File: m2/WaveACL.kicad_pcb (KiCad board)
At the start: 4 copper layers, 48 x 21 mm, 20 parts, among them J1 Conn_01x05, J2 Conn_01x02, J3 Conn_01x02, J4 Conn_01x02, J5 Conn_01x02, U1 LED2000, U2 LPC812M001JDH16

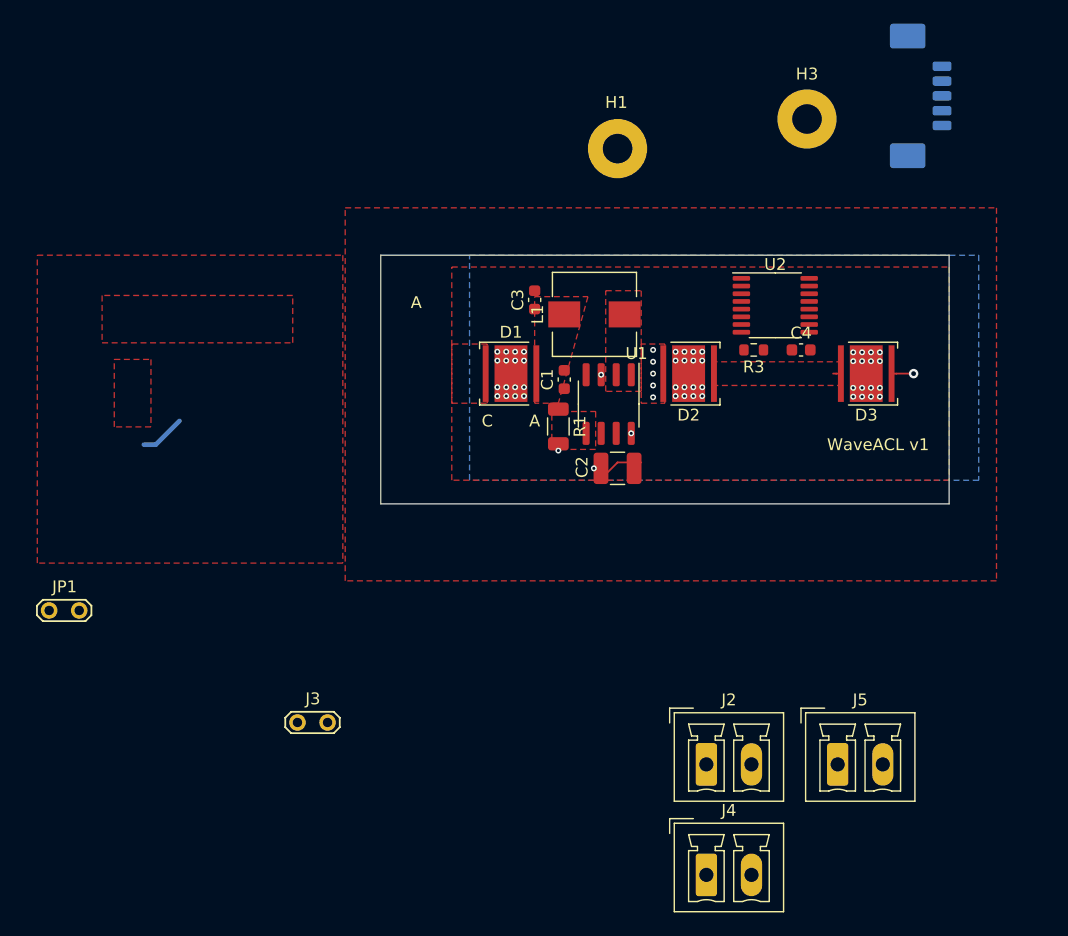
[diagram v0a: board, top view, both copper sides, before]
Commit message: Mark2 updates
- add I2C temp. sensor
- add voltage regulator for uC
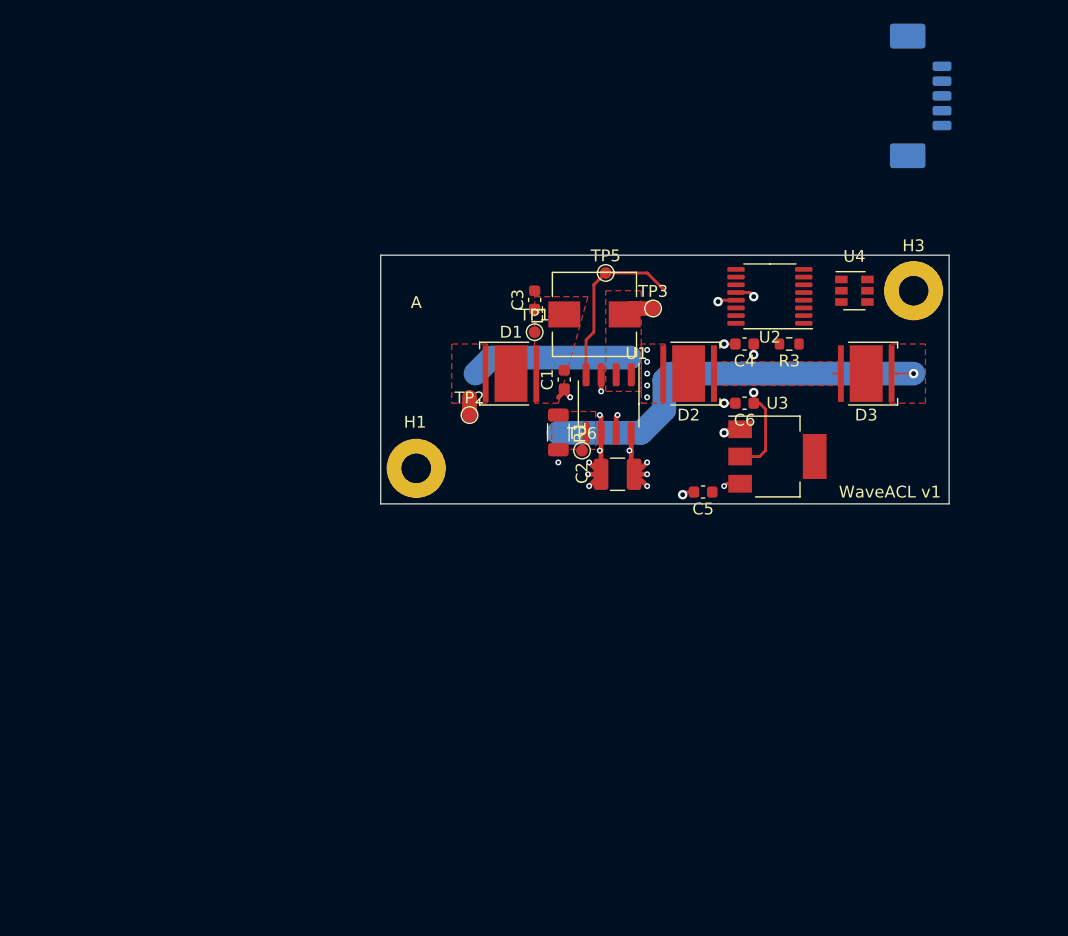
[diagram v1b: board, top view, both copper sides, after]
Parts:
- removed J2, J4, J5: Conn_01x02, Connector_Phoenix_MC:PhoenixContact_MCV_1,5_2-G-3.81_1x02_P3.81mm_Vertical
- removed J3: Conn_01x02, TestPoint:TestPoint_2Pads_Pitch2.54mm_Drill0.8mm
- removed JP1: Jumper_NO_Small, TestPoint:TestPoint_2Pads_Pitch2.54mm_Drill0.8mm
- added C5: 100n, Capacitor_SMD:C_0603_1608Metric, F.Cu at (165.2, 49.0)
- added C6: 100n, Capacitor_SMD:C_0603_1608Metric, F.Cu at (168.7, 41.5)
- added TP1: TestPoint, TestPoint:TestPoint_Pad_D1.0mm, F.Cu at (151.0, 35.5)
- added TP2: TestPoint, TestPoint:TestPoint_Pad_D1.0mm, F.Cu at (145.5, 42.5)
- added TP3: TestPoint, TestPoint:TestPoint_Pad_D1.0mm, F.Cu at (161.0, 33.5)
- added TP5: TestPoint, TestPoint:TestPoint_Pad_D1.0mm, F.Cu at (157.0, 30.5)
- added TP6: TestPoint, TestPoint:TestPoint_Pad_D1.0mm, F.Cu at (155.0, 45.5)
- added U3: LD1117S33TR_SOT223, Package_TO_SOT_SMD:SOT-223-3_TabPin2, F.Cu at (171.5, 46.0)
- added U4: TMP100, Package_TO_SOT_SMD:SOT-23-6, F.Cu at (178.0, 32.0)
- D1, D2, D3: footprint LED_SMD:LED_Cree-XHP50_6V -> fkl-footprints:LED_Cree-XHP50_6V
- moved H1 31.9 mm to (141.0, 47.0)
- moved H3 17.1 mm to (183.0, 32.0)
- moved C4 4.80 mm to (168.7, 36.5), turned to 180 degrees
- moved R3 3.04 mm to (172.5, 36.5)
- moved U2 0.88 mm to (170.9, 32.5), turned to 180 degrees
- moved C2 0.50 mm to (158.0, 47.5)
- moved R1 0.50 mm to (153.0, 44.0)
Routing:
- net /LED-: track 1.86 -> 35.4 mm
- net +3V3: track 0.00 -> 19.0 mm, vias 0 -> 3
- net VCC: track 4.60 -> 19.5 mm, vias 2 -> 7
- net PWM: track 0.00 -> 14.9 mm
- net (no net): track 0.00 -> 13.6 mm
- net GND: track 7.50 -> 16.2 mm, vias 50 -> 12
- net Net-(J3-Pad1): track 3.41 -> 0.00 mm
- net Net-(L1-Pad1): track 0.00 -> 2.61 mm
- net Net-(D1-Pad1): track 0.00 -> 1.50 mm
- added copper zone on F.Cu, net (none)
- added copper zone on In2.Cu, net VCC
- removed copper zone on B.Cu, net /HS1
- removed copper zone on F.Cu, net /HS1
- removed copper zone on F.Cu, net GND
- removed copper zone on In1.Cu, net GND
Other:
- board text removed: "C"

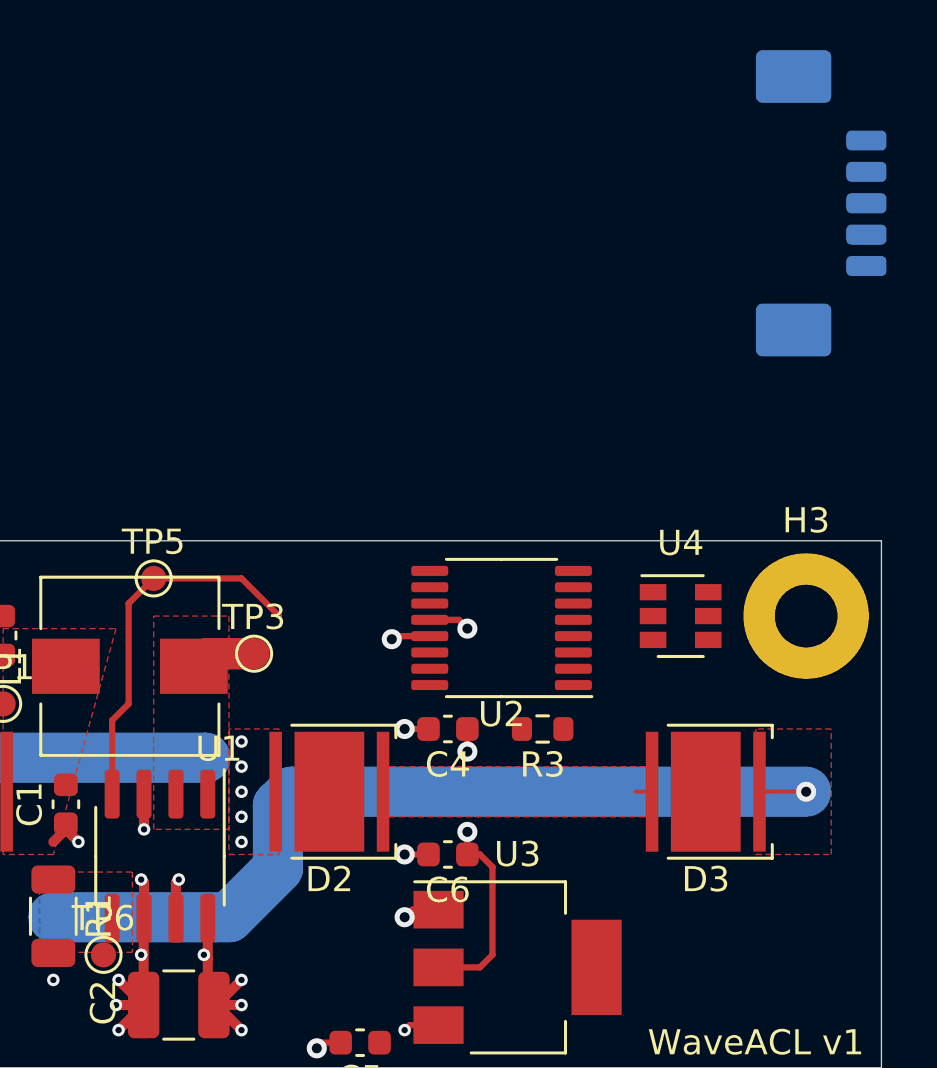
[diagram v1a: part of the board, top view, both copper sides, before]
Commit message: add SOICByte Footprint
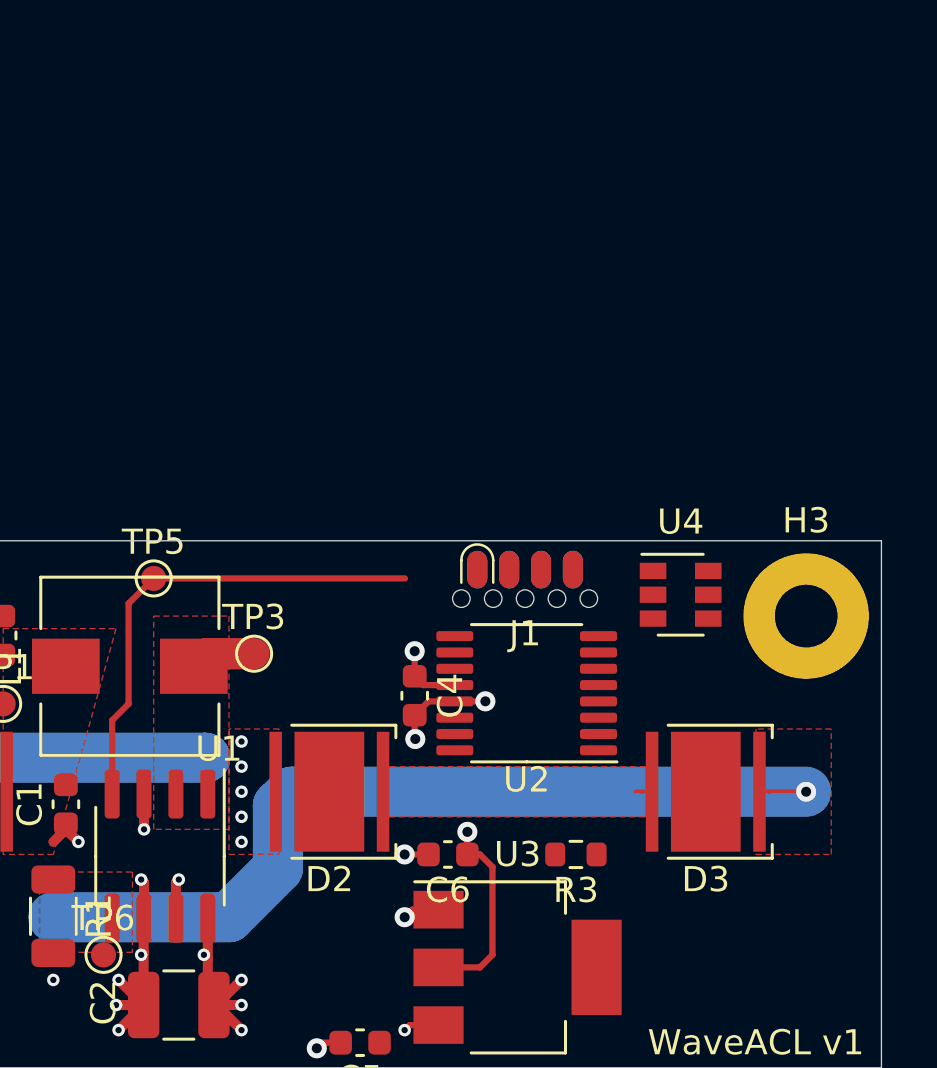
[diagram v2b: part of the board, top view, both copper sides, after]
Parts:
- J1: value Conn_01x05 -> Conn_01x08; footprint Connector_Molex:Molex_PicoBlade_53261-0571_1x05-1MP_P1.25mm_Horizontal -> fkl-footprints:Connector_SOICbite; moved to F.Cu
- moved J1 17.8 mm to (171.8, 29.4), turned to 180 degrees
- moved R3 5.17 mm to (173.8, 41.5)
- moved U2 2.79 mm to (171.9, 35.1)
- moved C4 1.87 mm to (167.4, 35.2), turned to 270 degrees
- moved U4 0.85 mm to (178.0, 31.1)
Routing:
- net PWM: track 14.9 -> 19.3 mm
- net GND: track 16.2 -> 17.7 mm
- net +3V3: vias 3 -> 2

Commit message: update m2
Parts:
- added C7: 100n, Capacitor_SMD:C_0603_1608Metric, F.Cu at (178.0, 34.0)
- C1: value 100n -> 1u
- D1, D2, D3: footprint fkl-footprints:LED_Cree-XHP50_6V -> fkl-footprints:LED_Cree-XLAMP-XM-L
- J1: value Conn_01x08 -> SOICBite
- moved TP1 4.92 mm to (146.5, 33.5)
- moved C3 1.95 mm to (151.0, 34.7)
- moved C1 0.27 mm to (153.5, 39.2)
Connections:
- J1 pad 1: /VTREF -> +3V3
- J1 pad 2: /SWDIO -> /RXD
- J1 pad 3: /SWCLK -> /TXD
- J1 pad 4: /~RESET -> GND
- J1 pad 5: GND -> /SWDIO
- J1 pad 7: Net-(J1-Pad7) -> /SWCLK
- J1 pad 8: Net-(J1-Pad8) -> /~RESET
- U4 pad 1: Net-(U4-Pad1) -> /SCK
- U4 pad 2: Net-(U4-Pad2) -> GND
- U4 pad 4: Net-(U4-Pad4) -> +3V3
- U4 pad 6: Net-(U4-Pad6) -> /SDA
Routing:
- net /~RESET: track 0.00 -> 9.41 mm, vias 0 -> 1
- net /SWCLK: track 0.00 -> 7.72 mm, vias 0 -> 1
- net GND: track 17.7 -> 23.7 mm, vias 12 -> 13
- net /SWDIO: track 0.00 -> 4.89 mm, vias 0 -> 1
- net PWM: track 19.3 -> 22.2 mm
- net +3V3: track 19.0 -> 20.7 mm
- net (no net): track 13.6 -> 14.1 mm
- net Net-(D1-Pad1): vias 5 -> 0
- added copper zone on F.Cu, net GND
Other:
- board text added: "WaveACL m2r0"
- board text removed: "WaveACL v1"

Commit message: updates
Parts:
- moved TP3 55.9 mm to (111.5, 59.5), turned to 180 degrees
- moved TP5 51.3 mm to (109.5, 50.0), turned to 180 degrees
- moved H1 30.3 mm to (171.0, 43.0)
- moved H3 29.2 mm to (156.0, 43.0)
- moved C2 25.2 mm to (139.0, 31.0), turned to 0 degrees
- moved C4 18.8 mm to (185.8, 38.9), turned to 180 degrees
- moved U1 18.1 mm to (139.8, 36.9), turned to 90 degrees
- moved TP6 18.0 mm to (142.0, 33.0), turned to 180 degrees
- moved L1 17.9 mm to (141.6, 44.5), turned to 0 degrees
- moved U4 16.0 mm to (179.8, 47.0), turned to 270 degrees
- moved C6 15.5 mm to (184.2, 41.0)
- moved R3 15.5 mm to (189.3, 41.0)
- moved U3 15.5 mm to (187.0, 45.5)
- moved J1 15.5 mm to (187.3, 29.4)
- moved U2 15.3 mm to (187.2, 35.1)
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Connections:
- H1 pad 1: /HS1 -> GND
- H3 pad 1: /HS1 -> GND
- U4 pad 3: Net-(U4-Pad3) -> GND
- U4 pad 5: Net-(U4-Pad5) -> GND
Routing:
- net /LED-: track 35.4 -> 13.1 mm, vias 1 -> 0
- net PWM: track 22.2 -> 8.74 mm
- net Net-(D2-Pad1): track 0.66 -> 11.4 mm
- net Net-(D1-Pad1): track 1.50 -> 10.7 mm
- net +3V3: track 20.7 -> 11.6 mm, vias 2 -> 1
- net GND: track 23.7 -> 18.2 mm, vias 13 -> 291
- net Net-(L1-Pad1): track 2.61 -> 0.71 mm
- net (no net): track 14.1 -> 12.9 mm
- removed copper zone on F.Cu, net (none)
- removed copper zone on F.Cu, net Net-(D1-Pad1)
- removed copper zone on F.Cu, net Net-(D2-Pad1)
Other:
- board size 48 x 21 mm -> 55 x 20 mm
- net class Default: clearance 0.2 -> 0.15
- net class current: clearance 0.2 -> 0.15; trace_width 1.25 -> 0.5
- rule trace_clearance: 0.2 -> 0.15
- rule via_min_size: 0.5 -> 0.6
- board text added: "WaveACL m2r1"
- board text removed: "WaveACL m2r0"

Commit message: update
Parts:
- added R2: R, Resistor_SMD:R_0603_1608Metric, F.Cu at (187.0, 41.8)
- added R4: R, Resistor_SMD:R_0603_1608Metric, F.Cu at (188.5, 41.8)
- added R5: R, Resistor_SMD:R_0603_1608Metric, F.Cu at (155.6, 54.9)
- added R6: R, Resistor_SMD:R_0603_1608Metric, F.Cu at (159.6, 54.9)
- added TP4: TestPoint, TestPoint:TestPoint_Pad_D1.0mm, F.Cu at (171.0, 39.0)
- added TP7: TestPoint, TestPoint:TestPoint_Pad_D1.0mm, F.Cu at (184.2, 41.5)
- U3: value LD1117S33TR_SOT223 -> TPS7A0533PDBV; footprint Package_TO_SOT_SMD:SOT-223-3_TabPin2 -> Package_TO_SOT_SMD:SOT-23-5
- U4: value TMP100 -> LM75B; footprint Package_TO_SOT_SMD:SOT-23-6 -> Package_DFN_QFN:DFN-8-1EP_3x2mm_P0.5mm_EP1.3x1.5mm
- moved TP5 37.6 mm to (147.0, 48.0)
- moved TP3 31.3 mm to (137.5, 42.0)
- moved C5 19.4 mm to (184.0, 46.5), turned to 270 degrees
- moved C6 7.98 mm to (190.0, 46.5), turned to 270 degrees
- moved C7 1.80 mm to (175.5, 46.0)
- moved U4 1.68 mm to (178.5, 46.0), turned to 180 degrees
- moved R3 1.05 mm to (190.0, 41.8), turned to 90 degrees
- moved U3 1.00 mm to (187.0, 46.5)
- moved C4 0.86 mm to (185.0, 39.0)
- moved C2 0.50 mm to (139.5, 31.0)
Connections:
- U3 pad 1: GND -> VCC
- U3 pad 2: +3V3 -> GND
- U3 pad 3: VCC -> Net-(U3-Pad3)
- U4 pad 1: /SCK -> /SDA
- U4 pad 2: GND -> /SCK
- U4 pad 3: GND -> Net-(R6-Pad2)
- U4 pad 4: +3V3 -> GND
- U4 pad 6: /SDA -> GND
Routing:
- net PWM: track 8.74 -> 53.7 mm, vias 0 -> 2
- net /SDA: track 0.00 -> 22.1 mm
- net /SCK: track 0.00 -> 21.5 mm
- net (no net): track 12.9 -> 0.00 mm
- net VCC: track 19.5 -> 11.6 mm, vias 7 -> 6
- net /SWCLK: track 7.72 -> 0.00 mm, vias 1 -> 0
- net /SWDIO: track 4.89 -> 0.00 mm, vias 1 -> 0
- net +3V3: track 11.6 -> 8.31 mm, vias 1 -> 9
- net GND: track 18.2 -> 17.2 mm, vias 291 -> 292
- net /~RESET: track 9.41 -> 9.42 mm, vias 1 -> 0
- added copper zone on In2.Cu, net +3V3
- added copper zone on B.Cu, net GND
- added copper zone on In1.Cu, net GND
- added copper zone on In2.Cu, net GND

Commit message: update
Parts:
- added D4: LED_RABG, LED_SMD:LED_Kingbright_AAA3528ESGCT, B.Cu at (179.4, 31.3)
- added J4: Screw_Terminal_01x02, Connector_Phoenix_MC:PhoenixContact_MCV_1,5_2-G-3.81_1x02_P3.81mm_Vertical, F.Cu at (130.5, 56.0)
- added R7: R, Resistor_SMD:R_0603_1608Metric, B.Cu at (174.0, 31.2)
- added R8: R, Resistor_SMD:R_0603_1608Metric, B.Cu at (176.0, 31.2)
- added R9: R, Resistor_SMD:R_0603_1608Metric, B.Cu at (182.5, 31.2)
- added TP11: TestPoint, TestPoint:TestPoint_Pad_D1.0mm, B.Cu at (190.0, 33.0)
- added TP7: TestPoint, TestPoint:TestPoint_Pad_D1.0mm, B.Cu at (190.0, 35.0)
- added TP8: TestPoint, TestPoint:TestPoint_Pad_D1.0mm, B.Cu at (190.0, 37.0)
- added TP9: TestPoint, TestPoint:TestPoint_Pad_D1.0mm, B.Cu at (190.0, 39.0)
- moved R6 24.1 mm to (182.5, 47.3), turned to 90 degrees
- moved TP10 0.50 mm to (184.2, 41.0)
- renumbered TP7 to TP10
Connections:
- J1 pad 6: Net-(J1-Pad6) -> /GPIO
- U2 pad 10: Net-(U2-Pad10) -> /LED_B
- U2 pad 11: Net-(U2-Pad11) -> /LED_G
- U2 pad 14: Net-(U2-Pad14) -> /LED_R
- U2 pad 4: Net-(U2-Pad4) -> /GPIO
- U3 pad 3: Net-(U3-Pad3) -> VCC
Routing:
- net Net-(R6-Pad2): track 0.00 -> 4.90 mm, vias 0 -> 2
- net /SDA: track 22.1 -> 19.2 mm
- net +3V3: track 8.31 -> 10.4 mm, vias 9 -> 10
- net /SCK: track 21.5 -> 22.2 mm
- net GND: track 17.2 -> 18.0 mm, vias 292 -> 293
